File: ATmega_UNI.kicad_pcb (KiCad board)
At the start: 2 copper layers, 53.3 x 68.6 mm, 60 parts, among them J1 PDIP_1_to_14, J11 PDIP_1_to_14, J2 PDIP_15_to_28, J22 PDIP_15_to_28, J611 I2C, J612 I2C, J613 I2C, J62 4uni, J63 4uni, J64 4uni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

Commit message: version++
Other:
- board text added: "meon.eu/191105"
- board text removed: "meon.eu/191020"
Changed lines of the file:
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@@
   (gr_line (start 106.68 88.9) (end 109.22 88.9) (layer B.SilkS) (width 0.2))
   (gr_line (start 106.68 88.9) (end 109.22 88.9) (layer F.SilkS) (width 0.2))
-  (gr_text meon.eu/191020 (at 82.804 113.03) (layer F.SilkS)
+  (gr_text meon.eu/191105 (at 82.804 113.03) (layer F.SilkS)
     (effects (font (size 0.9 0.9) (thickness 0.2)))
   )
@@
     (effects (font (size 0.7 0.7) (thickness 0.15)))
   )
-  (gr_text meon.eu/191020 (at 82.804 113.03) (layer B.SilkS)
+  (gr_text meon.eu/191105 (at 82.804 113.03) (layer B.SilkS)
     (effects (font (size 0.9 0.9) (thickness 0.2)) (justify mirror))
   )

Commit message: tidy-up
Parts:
- C2: value 0.1uF -> 100nF
- moved C14 5.08 mm to (81.3, 106.7), turned to 90 degrees
- moved SW1 0.51 mm to (85.1, 55.9)
- moved R2 0.23 mm to (93.3, 58.5)
- moved R22 0.23 mm to (95.2, 58.5)
- moved C22 0.15 mm to (90.2, 55.9)
- moved C2 0.13 mm to (92.7, 55.9)
- turned C12 to 90 degrees
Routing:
- net XTAL2: track 31.0 -> 35.1 mm
- net GND: track 406.0 -> 403.4 mm
- net ~RST: track 84.7 -> 85.2 mm
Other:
- board text added: "meon.eu/191125"
- board text removed: "meon.eu/191105"

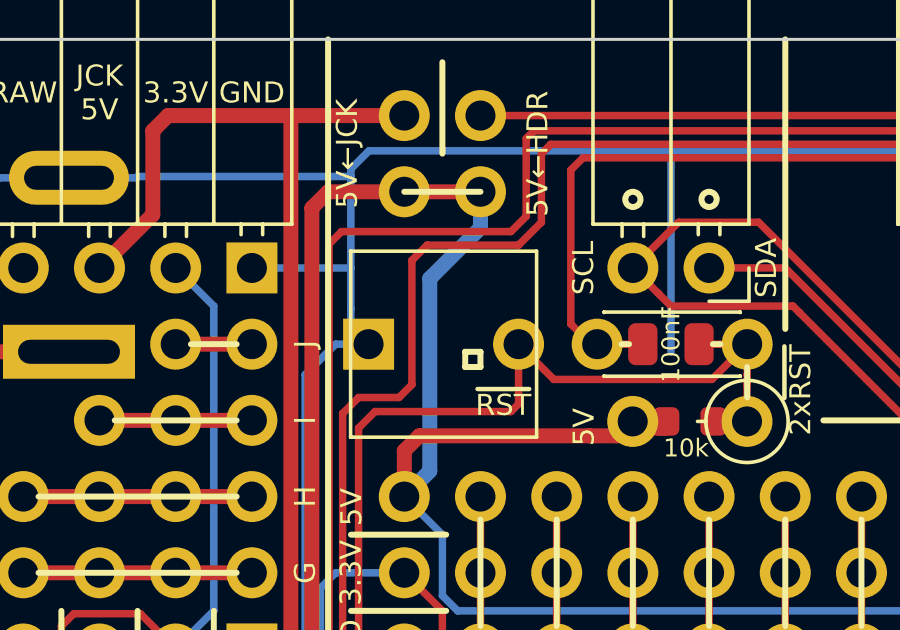
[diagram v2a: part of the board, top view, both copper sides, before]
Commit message: add sd reset switch
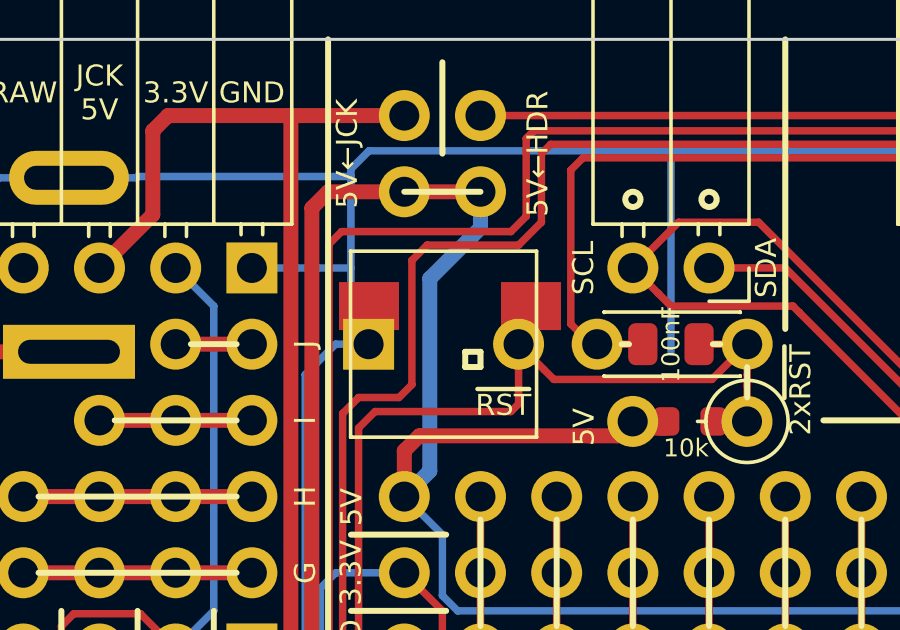
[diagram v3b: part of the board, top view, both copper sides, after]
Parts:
- added SW2: Reset, Button_Switch_SMD:SW_SPST_EVQPE1_no_lines, F.Cu at (85.3, 54.6)
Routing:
- net GND: track 403.4 -> 405.9 mm
- net ~RST: track 85.2 -> 86.9 mm
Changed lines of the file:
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@@
     (thickness 1.6)
     (drawings 572)
-    (tracks 748)
+    (tracks 754)
     (zones 0)
-    (modules 60)
+    (modules 61)
     (nets 72)
   )
@@
       (effects (font (size 1 1) (thickness 0.15)))
     )
-    (fp_text user %R (at 0 0 180) (layer F.Fab)
+    (fp_text user %R (at 0 0 180) (layer F.Fab) hide
       (effects (font (size 1 1) (thickness 0.15)))
     )
@@
       (net 25 ~RST))
   )
+  (module Button_Switch_SMD:SW_SPST_EVQPE1_no_lines (layer F.Cu)
+    (at 85.344 54.61 180)
+    (descr "Light Touch Switch, https://industrial.panasonic.com/cdbs/www-data/pdf/ATK0000/ATK0000CE7.pdf")
+    (attr smd)
+    (fp_text reference SW2 (at 0 -2.65 180) (layer F.SilkS) hide
+      (effects (font (size 1 1) (thickness 0.15)))
+    )
+    (fp_text value Reset (at 0 3 180) (layer F.Fab)
+      (effects (font (size 1 1) (thickness 0.15)))
+    )
+    (fp_text user %R (at 0 -2.65 180) (layer F.Fab) hide
+      (effects (font (size 1 1) (thickness 0.15)))
+    )
+    (fp_line (start 3 -1.75) (end 3 1.75) (layer F.Fab) (width 0.1))
+    (fp_line (start 3 1.75) (end -3 1.75) (layer F.Fab) (width 0.1))
+    (fp_line (start -3 1.75) (end -3 -1.75) (layer F.Fab) (width 0.1))
+    (fp_line (start -3 -1.75) (end 3 -1.75) (layer F.Fab) (width 0.1))
+    (fp_line (start -1.4 -0.7) (end 1.4 -0.7) (layer F.Fab) (width 0.1))
+    (fp_line (start 1.4 -0.7) (end 1.4 0.7) (layer F.Fab) (width 0.1))
+    (fp_line (start 1.4 0.7) (end -1.4 0.7) (layer F.Fab) (width 0.1))
+    (fp_line (start -1.4 0.7) (end -1.4 -0.7) (layer F.Fab) (width 0.1))
+    (fp_line (start -3.95 -2) (end 3.95 -2) (layer F.CrtYd) (width 0.05))
+    (fp_line (start 3.95 -2) (end 3.95 2) (layer F.CrtYd) (width 0.05))
+    (fp_line (start 3.95 2) (end -3.95 2) (layer F.CrtYd) (width 0.05))
+    (fp_line (start -3.95 2) (end -3.95 -2) (layer F.CrtYd) (width 0.05))
+    (pad 2 smd rect (at 2.7 0 180) (size 2 1.6) (layers F.Cu F.Paste F.Mask)
+      (net 24 GND))
+    (pad 1 smd rect (at -2.7 0 180) (size 2 1.6) (layers F.Cu F.Paste F.Mask)
+      (net 25 ~RST))
+    (model ${KISYS3DMOD}/Button_Switch_SMD.3dshapes/SW_SPST_EVQPE1.wrl
+      (at (xyz 0 0 0))
+      (scale (xyz 1 1 1))
+      (rotate (xyz 0 0 0))
+    )
+  )
   (gr_line (start 81.28 102.743) (end 81.28 102.489) (layer F.SilkS) (width 0.2))
   (gr_line (start 81.28 105.537) (end 81.28 105.791) (layer F.SilkS) (width 0.2))
@@
   (segment (start 81.53 55.88) (end 80.518 56.892) (width 0.25) (layer B.Cu) (net 24))
   (segment (start 82.63 55.88) (end 81.53 55.88) (width 0.25) (layer B.Cu) (net 24))
+  (segment (start 82.63 55.88) (end 82.63 54.69) (width 0.25) (layer F.Cu) (net 24))
+  (segment (start 82.63 54.69) (end 82.804 54.864) (width 0.25) (layer F.Cu) (net 24))
+  (segment (start 82.804 54.864) (end 82.804 55.88) (width 0.25) (layer F.Cu) (net 24))
   (segment (start 85.09 71.12) (end 88.9 71.12) (width 0.25) (layer F.Cu) (net 25) (status 30))
   (segment (start 88.9 71.12) (end 91.44 71.12) (width 0.25) (layer F.Cu) (net 25) (status 30))
@@
   (segment (start 87.63 57.872) (end 87.376 58.126) (width 0.25) (layer F.Cu) (net 25))
   (segment (start 82.844 58.126) (end 87.376 58.126) (width 0.25) (layer F.Cu) (net 25))
+  (segment (start 87.63 54.677919) (end 87.697919 54.61) (width 0.25) (layer F.Cu) (net 25))
+  (segment (start 87.63 55.88) (end 87.63 54.677919) (width 0.25) (layer F.Cu) (net 25))
+  (segment (start 87.697919 54.61) (end 88.138 54.61) (width 0.25) (layer F.Cu) (net 25))
   (segment (start 88.9 73.66) (end 85.09 73.66) (width 0.25) (layer F.Cu) (net 26) (status 30))
   (segment (start 91.44 73.66) (end 88.9 73.66) (width 0.25) (layer F.Cu) (net 26) (status 30))

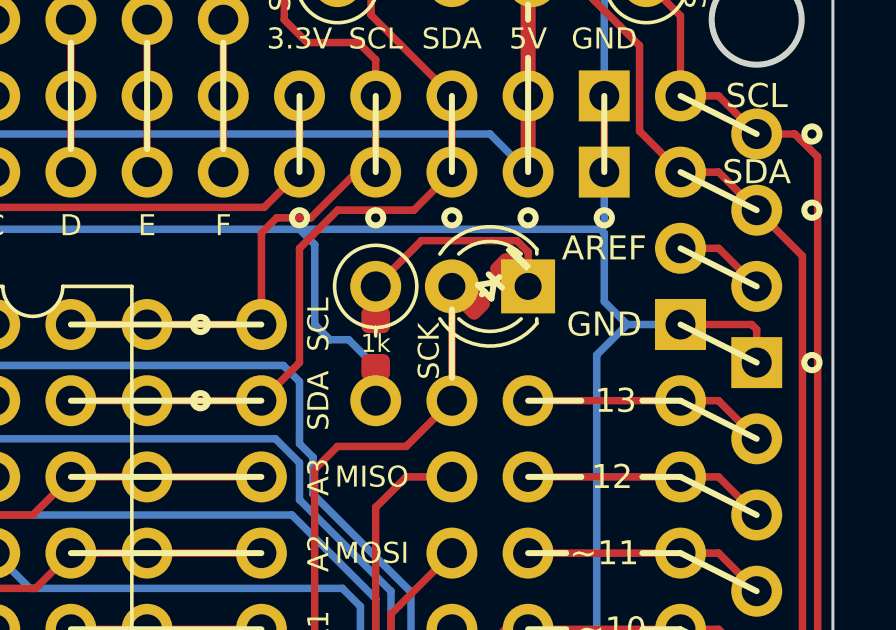
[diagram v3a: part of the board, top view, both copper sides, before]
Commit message: tidy-up pad shapes
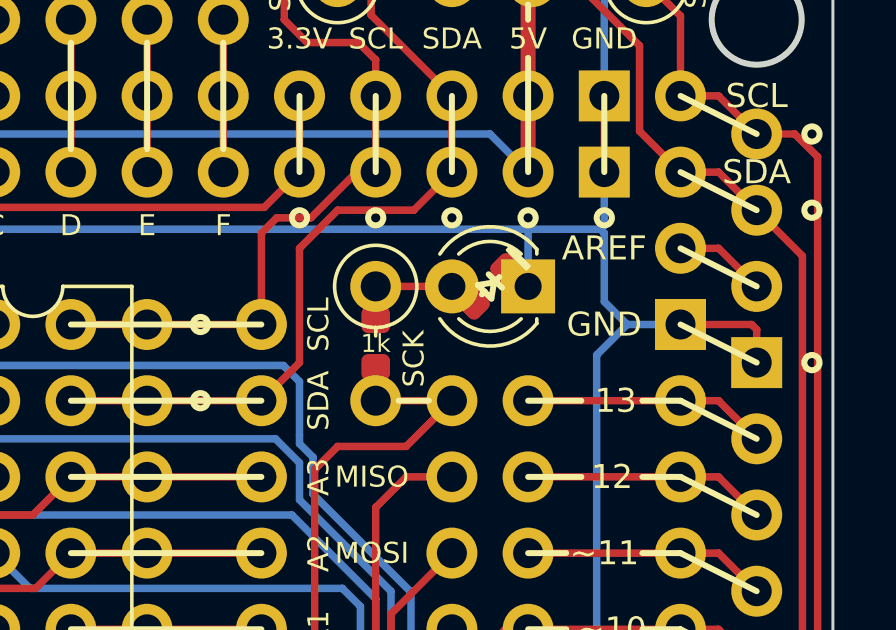
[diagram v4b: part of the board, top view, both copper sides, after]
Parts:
- D1, D92: footprint LED_THT:LED_D3.0mm -> LED_THT:LED_D3.0mm_doubleside
- turned R11 to 90 degrees
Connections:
- D1 pad 1: Net-(D1-Pad1) -> GND
- D1 pad 2: SCK -> Net-(D1-Pad2)
- D12 pad 1: Net-(D1-Pad1) -> GND
- D12 pad 2: SCK -> Net-(D1-Pad2)
- R11 pad 1: Net-(D1-Pad1) -> SCK
- R11 pad 2: GND -> Net-(D1-Pad2)
- R112 pad 1: Net-(D1-Pad1) -> Net-(D1-Pad2)
- R112 pad 2: GND -> SCK
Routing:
- net Net-(D1-Pad1): track 9.08 -> 0.00 mm
- net GND: track 405.9 -> 400.5 mm
- net Net-(D1-Pad2): track 0.00 -> 4.63 mm
- net SCK: track 54.3 -> 53.1 mm

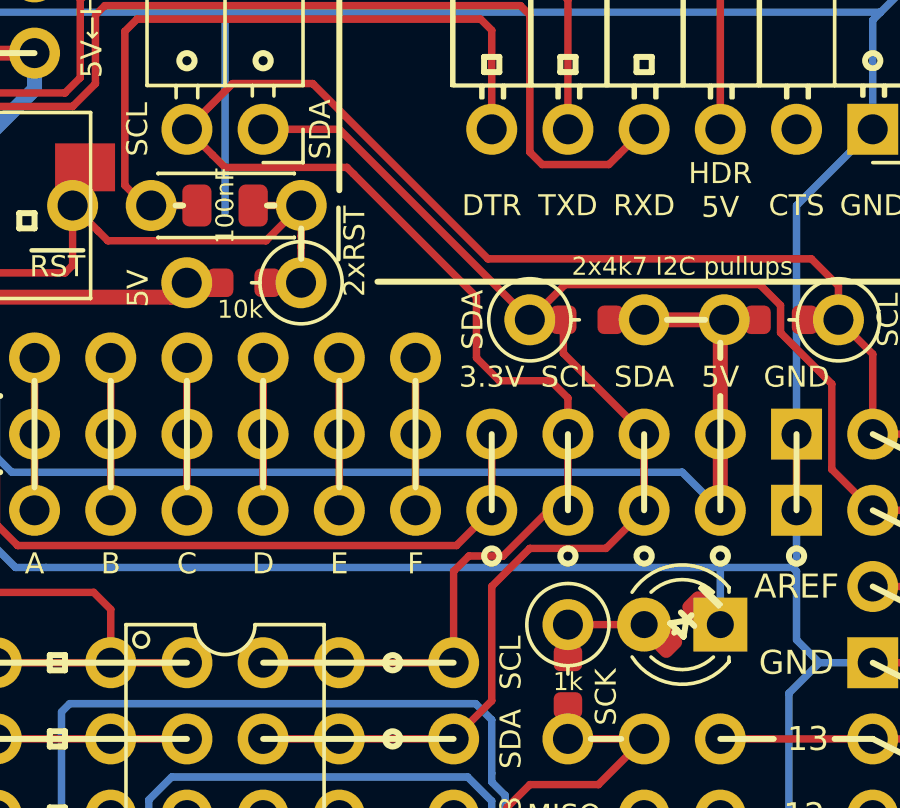
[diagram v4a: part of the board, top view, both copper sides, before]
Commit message: more b.sliks art
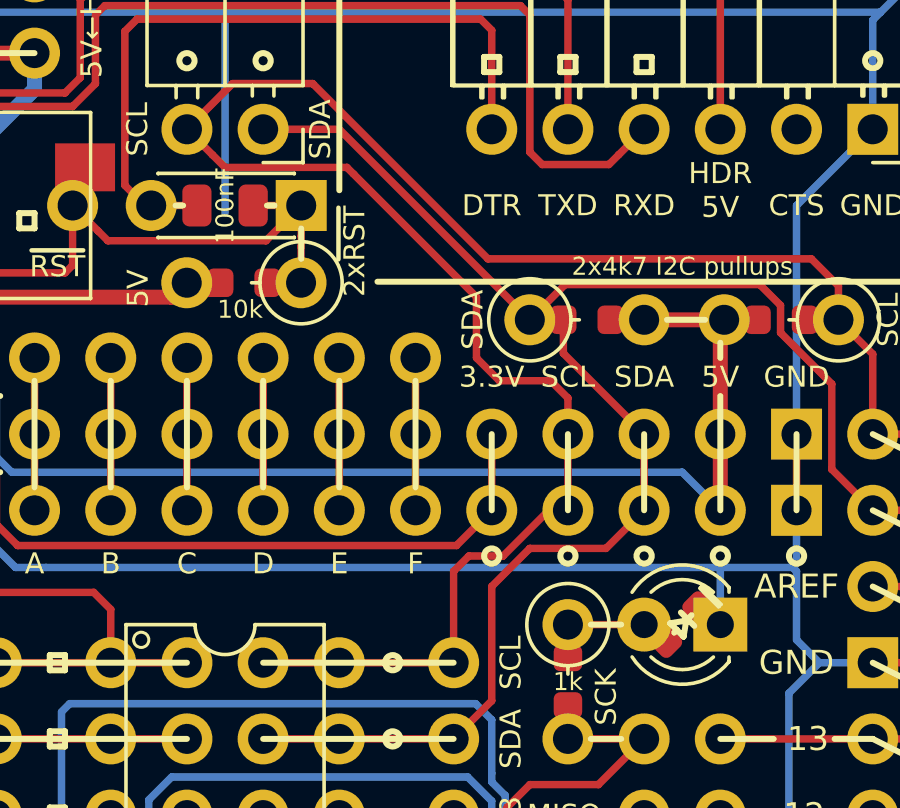
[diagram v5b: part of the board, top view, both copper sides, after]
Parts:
- C13, C14, C22: footprint Capacitor_THT:C_Disc_D4.3mm_W1.9mm_P5.00mm -> Capacitor_THT:C_Disc_D4.3mm_W1.9mm_P5.00mm_doubleside
- R112, R12, R22, R32, R92: footprint Resistor_THT:R_Axial_DIN0207_L6.3mm_D2.5mm_P3.81mm_Vertical -> Resistor_THT:R_Axial_DIN0207_L6.3mm_D2.5mm_P3.81mm_Vertical_doubleside

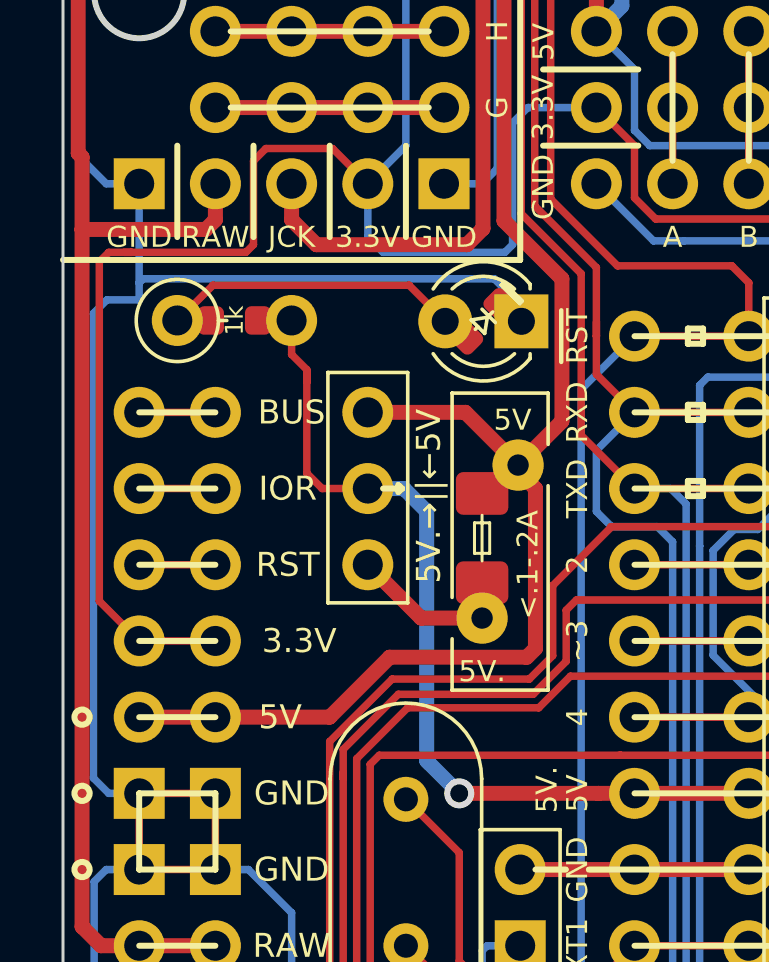
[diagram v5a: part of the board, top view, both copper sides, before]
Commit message: move pwr led and r
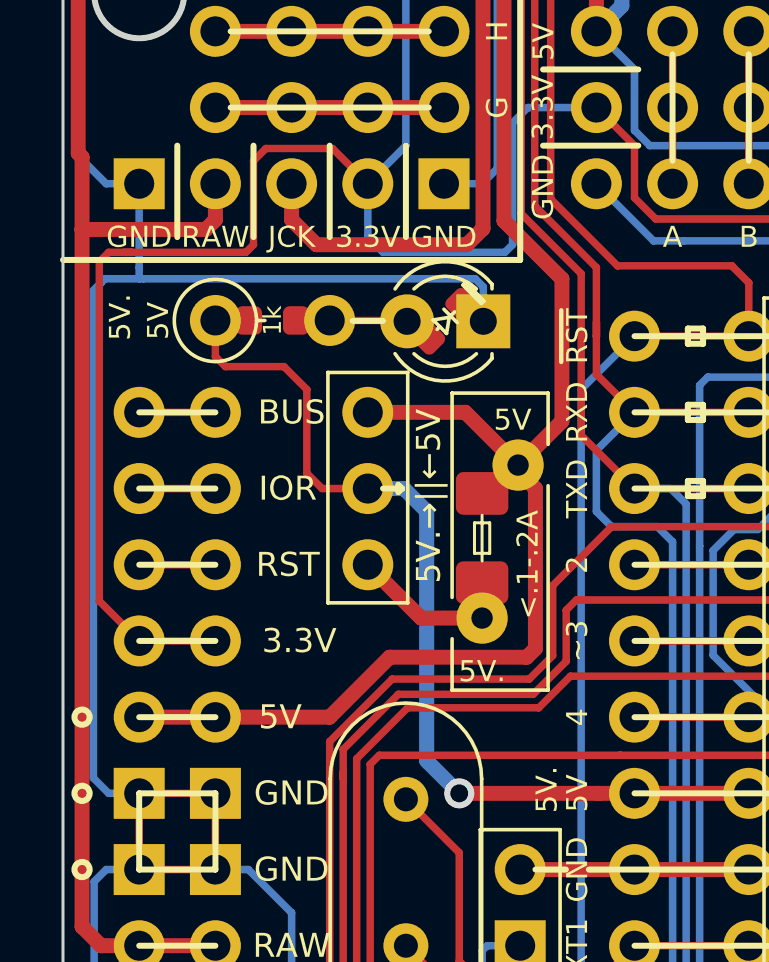
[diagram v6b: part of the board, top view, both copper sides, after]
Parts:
- moved D9 1.27 mm to (78.8, 70.6)
- moved R9 1.27 mm to (73.0, 70.6), turned to 180 degrees
- moved R92 1.27 mm to (71.1, 70.6)
- moved D92 1.27 mm to (80.1, 70.6)
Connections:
- R92 pad 1: Net-(D9-Pad2) -> +5V_jmp
- R92 pad 2: +5V_jmp -> Net-(D9-Pad2)
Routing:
- net Net-(D9-Pad2): track 12.0 -> 4.37 mm
- net +5V_jmp: track 65.6 -> 67.4 mm
